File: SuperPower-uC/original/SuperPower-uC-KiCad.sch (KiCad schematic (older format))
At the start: 0 parts

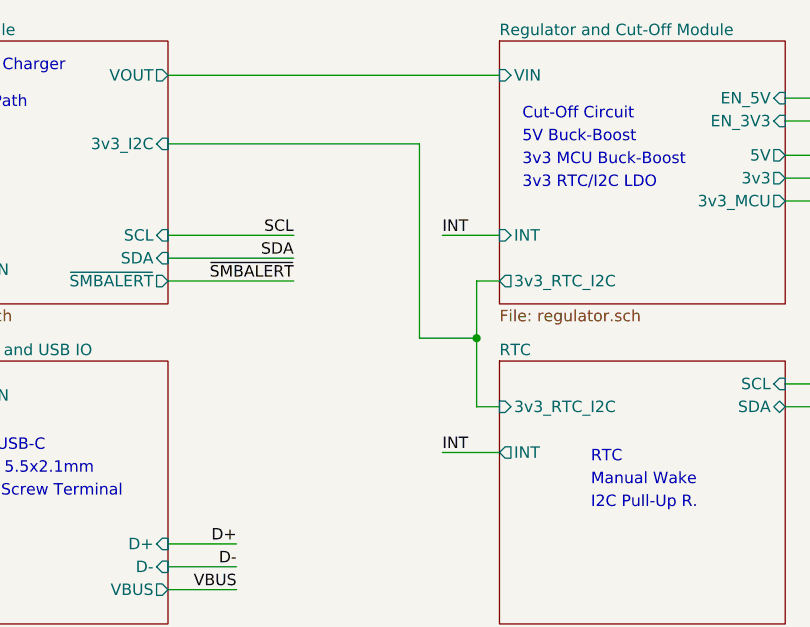
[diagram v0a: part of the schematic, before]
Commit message: Cleaned up the schematics and moved the I2C regulator to the RTC sheet
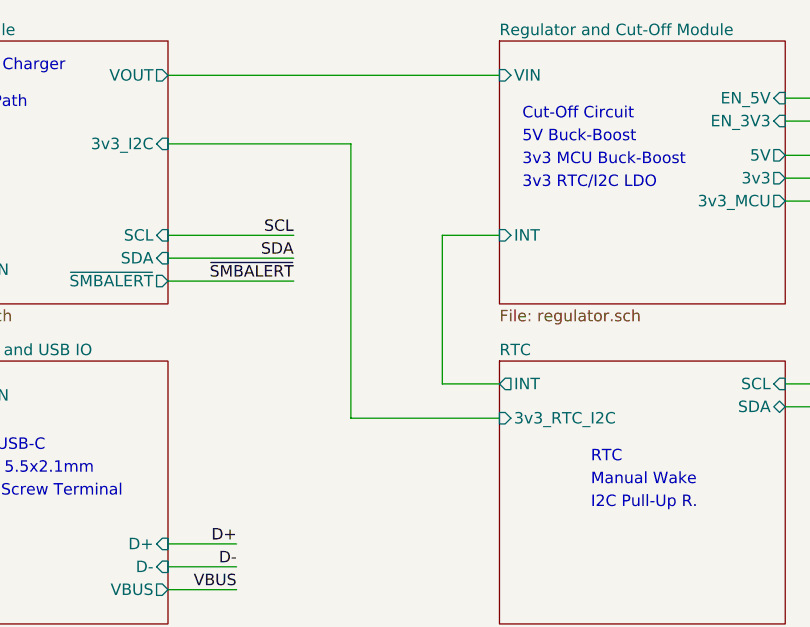
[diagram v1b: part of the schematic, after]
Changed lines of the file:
@@
 F2 "SCL" I R 7000 3600 50
 F3 "SDA" B R 7000 3700 50
-F4 "3v3_RTC_I2C" I L 5750 3700 50
-F5 "INT" O L 5750 3900 50
+F4 "3v3_RTC_I2C" I L 5750 3750 50
+F5 "INT" O L 5750 3600 50
 $EndSheet
 Wire Wire Line
@@
 Wire Wire Line
 	5750 2250 4300 2250
-Wire Wire Line
-	5400 2550 4300 2550
 Wire Wire Line
 	8600 2350 7000 2350
@@
 	10150 3150 9850 3150
 Wire Wire Line
-	5750 3700 5650 3700
-Wire Wire Line
-	5650 3700 5650 3400
-Wire Wire Line
-	5650 3150 5750 3150
-Wire Wire Line
-	5400 3400 5650 3400
-Wire Wire Line
-	5400 2550 5400 3400
-Connection ~ 5650 3400
-Wire Wire Line
-	5650 3400 5650 3150
-Text Label 5500 3900 0    50   ~ 0
-INT
-Wire Wire Line
-	5500 3900 5750 3900
-Text Label 5500 2950 0    50   ~ 0
-INT
+	5500 3600 5750 3600
 Wire Wire Line
 	5500 2950 5750 2950
@@
 F0 "Regulator and Cut-Off Module" 50
 F1 "regulator.sch" 50
-F2 "INT" I L 5750 2950 50
-F3 "3v3" O R 7000 2700 50
-F4 "5V" O R 7000 2600 50
-F5 "3v3_MCU" O R 7000 2800 50
-F6 "VIN" I L 5750 2250 50
-F7 "EN_3V3" I R 7000 2450 50
-F8 "EN_5V" I R 7000 2350 50
-F9 "3v3_RTC_I2C" O L 5750 3150 50
+F2 "3v3" O R 7000 2700 50
+F3 "5V" O R 7000 2600 50
+F4 "3v3_MCU" O R 7000 2800 50
+F5 "VIN" I L 5750 2250 50
+F6 "EN_3V3" I R 7000 2450 50
+F7 "EN_5V" I R 7000 2350 50
+F8 "INT" I L 5750 2950 50
 $EndSheet
 Text Notes 9100 2600 0    50   ~ 0
@@
 Text Notes 6150 4150 0    50   ~ 0
 I2C Pull-Up R.
+Wire Wire Line
+	5100 2550 4300 2550
+Wire Wire Line
+	5750 3750 5100 3750
+Wire Wire Line
+	5100 2550 5100 3750
+Wire Wire Line
+	5500 3600 5500 2950
 $EndSCHEMATC

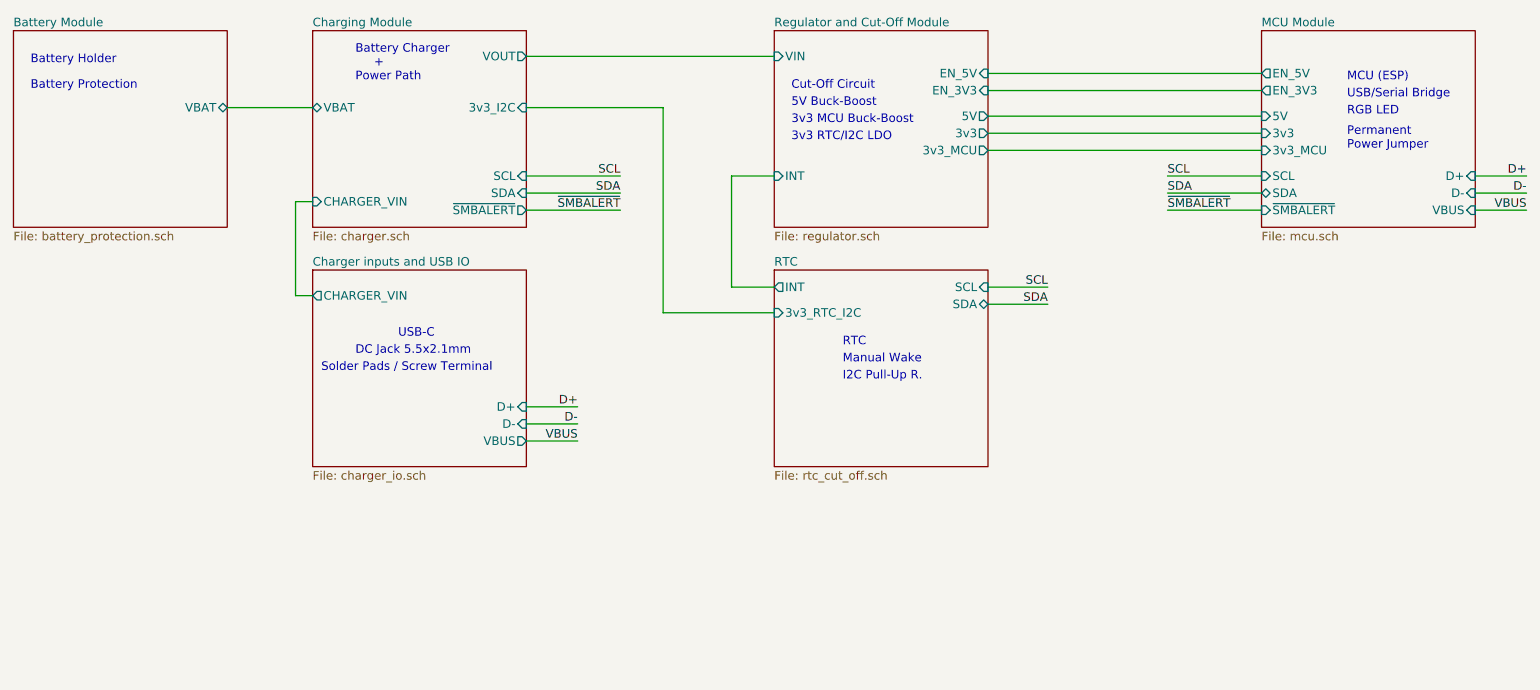
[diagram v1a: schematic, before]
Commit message: Layed out IO sheet parts
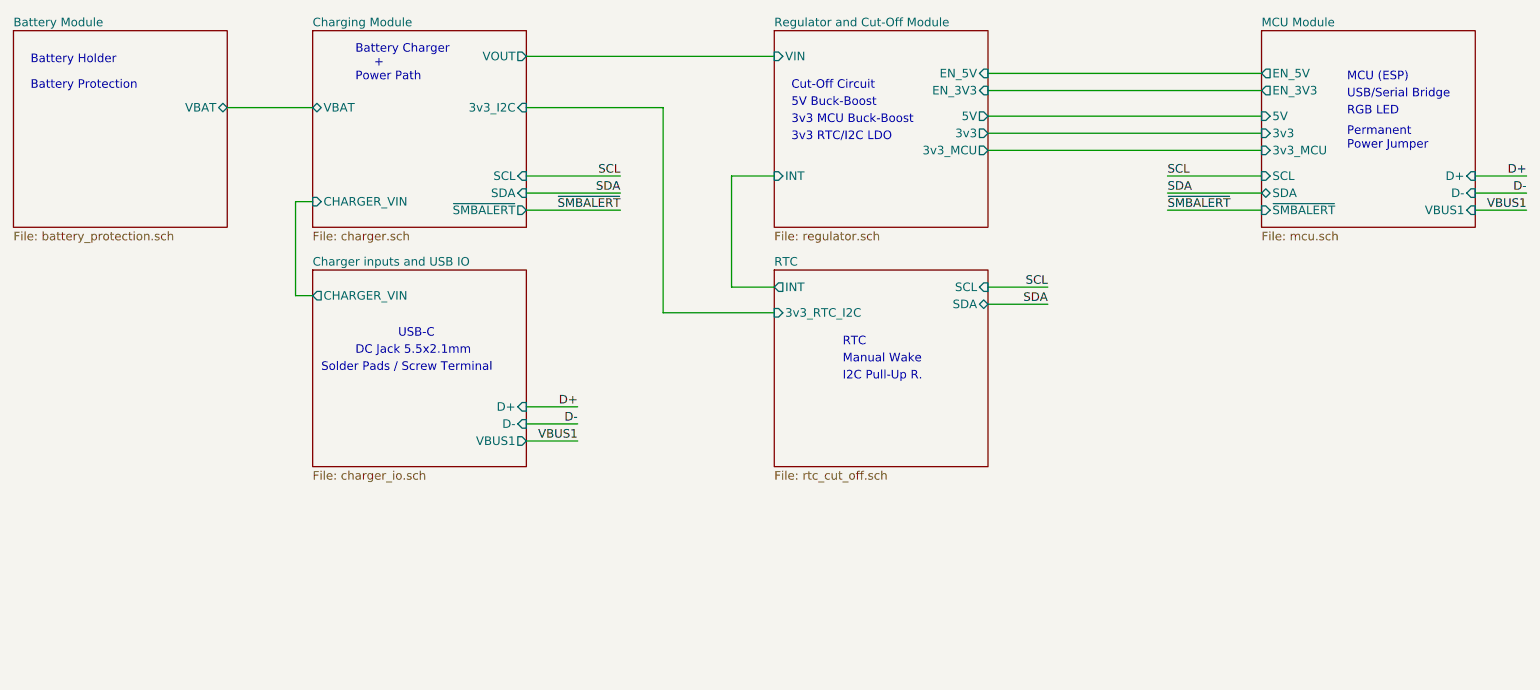
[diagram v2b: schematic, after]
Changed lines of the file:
@@
 F0 "Charger inputs and USB IO" 50
 F1 "charger_io.sch" 50
-F2 "VBUS" O R 4300 4500 50
-F3 "D+" I R 4300 4300 50
-F4 "D-" I R 4300 4400 50
-F5 "CHARGER_VIN" O L 3050 3650 50
+F2 "D+" I R 4300 4300 50
+F3 "D-" I R 4300 4400 50
+F4 "CHARGER_VIN" O L 3050 3650 50
+F5 "VBUS1" O R 4300 4500 50
 $EndSheet
 Wire Wire Line
@@
 	4850 3150 4300 3150
 Text Label 4600 4500 2    50   ~ 0
-VBUS
+VBUS1
 Text Label 4600 4400 2    50   ~ 0
 D-
@@
 	4600 4500 4300 4500
 Text Label 10150 3150 2    50   ~ 0
-VBUS
+VBUS1
 Text Label 10150 3050 2    50   ~ 0
 D-
@@
 F5 "D+" I R 9850 2950 50
 F6 "D-" I R 9850 3050 50
-F7 "VBUS" I R 9850 3150 50
-F8 "5V" I L 8600 2600 50
-F9 "3v3" I L 8600 2700 50
-F10 "EN_3V3" O L 8600 2450 50
-F11 "EN_5V" O L 8600 2350 50
-F12 "~SMBALERT" I L 8600 3150 50
+F7 "5V" I L 8600 2600 50
+F8 "3v3" I L 8600 2700 50
+F9 "EN_3V3" O L 8600 2450 50
+F10 "EN_5V" O L 8600 2350 50
+F11 "~SMBALERT" I L 8600 3150 50
+F12 "VBUS1" I R 9850 3150 50
 $EndSheet
 $Sheet

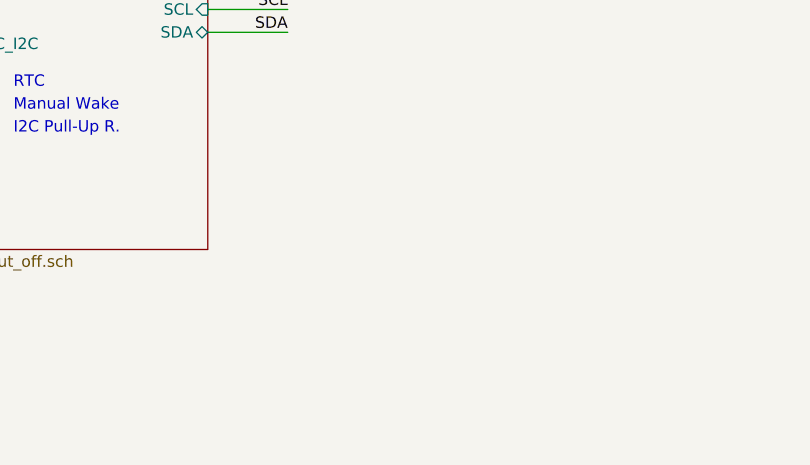
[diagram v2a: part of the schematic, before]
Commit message: draft of the squared stackable version
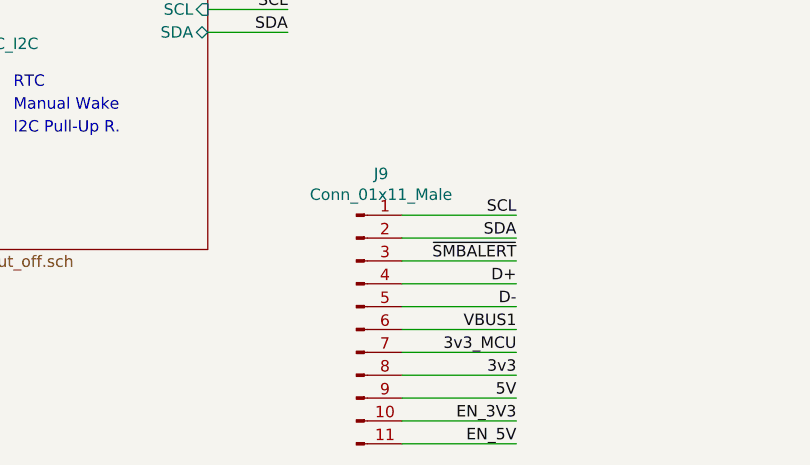
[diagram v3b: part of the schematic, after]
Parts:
- added J9: Conn_01x11_Male, Connector_PinSocket_2.54mm:PinSocket_1x11_P2.54mm_Vertical, symbol Connector:Conn_01x11_Male
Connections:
- net D+: now also J9.4 (Pin_4)
- net D-: now also J9.5 (Pin_5)
- net SCL: now also J9.1 (Pin_1)
- net SDA: now also J9.2 (Pin_2)
- net VBUS1: now also J9.6 (Pin_6)
- net ~SMBALERT: now also J9.3 (Pin_3)
- new net 3v3: J9.8 (Pin_8)
- new net 3v3_MCU: J9.7 (Pin_7)
- new net 5V: J9.9 (Pin_9)
- new net EN_3V3: J9.10 (Pin_10)
- new net EN_5V: J9.11 (Pin_11)
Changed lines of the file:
@@
 Wire Wire Line
 	5500 3600 5500 2950
+$Comp
+L Connector:Conn_01x11_Male J9
+U 1 1 60000B18
+P 7650 5000
+F 0 "J9" H 7758 5681 50  0000 C CNN
+F 1 "Conn_01x11_Male" H 7758 5590 50  0000 C CNN
+F 2 "Connector_PinSocket_2.54mm:PinSocket_1x11_P2.54mm_Vertical" H 7650 5000 50  0001 C CNN
+F 3 "~" H 7650 5000 50  0001 C CNN
+	1    7650 5000
+	1    0    0    -1
+$EndComp
+Text Label 8350 4500 2    50   ~ 0
+SCL
+Text Label 8350 4600 2    50   ~ 0
+SDA
+Text Label 8350 4700 2    50   ~ 0
+~SMBALERT
+Text Label 8350 4800 2    50   ~ 0
+D+
+Text Label 8350 4900 2    50   ~ 0
+D-
+Text Label 8350 5000 2    50   ~ 0
+VBUS1
+Text Label 8350 5200 2    50   ~ 0
+3v3
+Text Label 8350 5500 2    50   ~ 0
+EN_5V
+Text Label 8350 5400 2    50   ~ 0
+EN_3V3
+Text Label 8350 5300 2    50   ~ 0
+5V
+Text Label 8350 5100 2    50   ~ 0
+3v3_MCU
+Wire Wire Line
+	7850 4500 8350 4500
+Wire Wire Line
+	8350 4600 7850 4600
+Wire Wire Line
+	7850 4700 8350 4700
+Wire Wire Line
+	8350 4800 7850 4800
+Wire Wire Line
+	7850 4900 8350 4900
+Wire Wire Line
+	8350 5000 7850 5000
+Wire Wire Line
+	7850 5100 8350 5100
+Wire Wire Line
+	8350 5200 7850 5200
+Wire Wire Line
+	7850 5300 8350 5300
+Wire Wire Line
+	8350 5400 7850 5400
+Wire Wire Line
+	7850 5500 8350 5500
 $EndSCHEMATC

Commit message: Layed out the whole charger board
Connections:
- net 3v3: now also J9.10 (Pin_10); no longer J9.8 (Pin_8)
- net 3v3_MCU: now also J9.9 (Pin_9); no longer J9.7 (Pin_7)
- net 5V: now also J9.7 (Pin_7); no longer J9.9 (Pin_9)
- net EN_3V3: now also J9.8 (Pin_8); no longer J9.10 (Pin_10)
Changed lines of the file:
@@
 Text Label 8350 5000 2    50   ~ 0
 VBUS1
-Text Label 8350 5200 2    50   ~ 0
+Text Label 8350 5400 2    50   ~ 0
 3v3
 Text Label 8350 5500 2    50   ~ 0
 EN_5V
-Text Label 8350 5400 2    50   ~ 0
+Text Label 8350 5200 2    50   ~ 0
 EN_3V3
+Text Label 8350 5100 2    50   ~ 0
+5V
 Text Label 8350 5300 2    50   ~ 0
-5V
-Text Label 8350 5100 2    50   ~ 0
 3v3_MCU
 Wire Wire Line
@@
 Wire Wire Line
 	7850 5500 8350 5500
+Text Label 8300 2350 2    50   ~ 0
+EN_5V
+Text Label 8300 2450 2    50   ~ 0
+EN_3V3
+Text Label 8300 2600 2    50   ~ 0
+5V
+Text Label 8300 2700 2    50   ~ 0
+3v3
+Text Label 8300 2800 2    50   ~ 0
+3v3_MCU
 $EndSCHEMATC

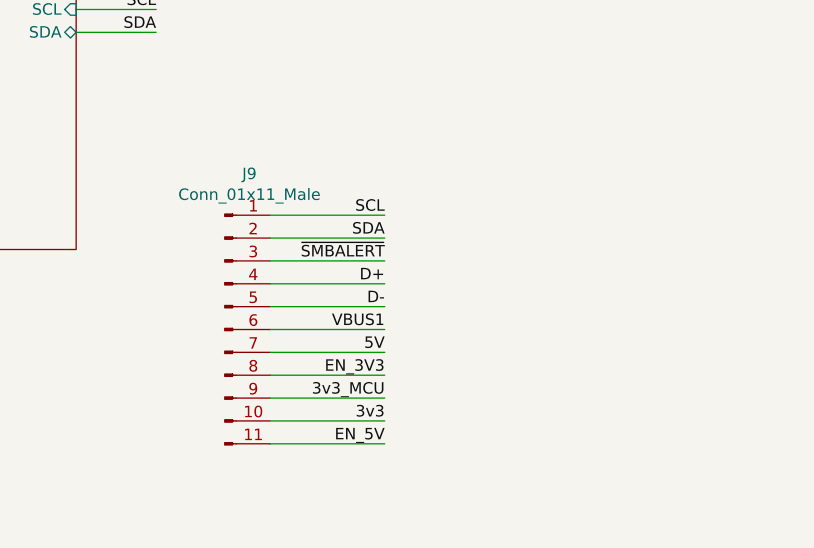
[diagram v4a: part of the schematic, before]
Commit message: Layed out mcu board
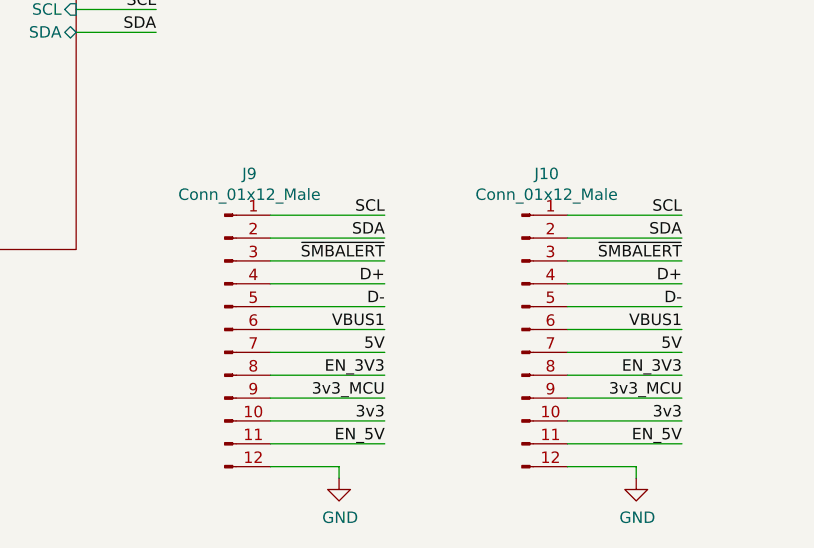
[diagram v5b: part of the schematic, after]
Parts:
- removed J9: Conn_01x11_Male, Connector_PinSocket_2.54mm:PinSocket_1x11_P2.54mm_Vertical, symbol Connector:Conn_01x11_Male
- added J10, J9: Conn_01x12_Male, Connector_PinSocket_2.54mm:PinSocket_1x12_P2.54mm_Vertical, symbol Connector:Conn_01x12_Male
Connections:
- net 3v3: now also J10.10 (Pin_10), J9.10 (Pin_10)
- net 3v3_MCU: now also J10.9 (Pin_9), J9.9 (Pin_9)
- net 5V: now also J10.7 (Pin_7), J9.7 (Pin_7)
- net D+: now also J10.4 (Pin_4), J9.4 (Pin_4)
- net D-: now also J10.5 (Pin_5), J9.5 (Pin_5)
- net EN_3V3: now also J10.8 (Pin_8), J9.8 (Pin_8)
- net EN_5V: now also J10.11 (Pin_11), J9.11 (Pin_11)
- net SCL: now also J10.1 (Pin_1), J9.1 (Pin_1)
- net SDA: now also J10.2 (Pin_2), J9.2 (Pin_2)
- net VBUS1: now also J10.6 (Pin_6), J9.6 (Pin_6)
- net ~SMBALERT: now also J10.3 (Pin_3), J9.3 (Pin_3)
- new net GND: J10.12 (Pin_12), J9.12 (Pin_12)
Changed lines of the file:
@@
 Wire Wire Line
 	5500 3600 5500 2950
-$Comp
-L Connector:Conn_01x11_Male J9
-U 1 1 60000B18
-P 7650 5000
-F 0 "J9" H 7758 5681 50  0000 C CNN
-F 1 "Conn_01x11_Male" H 7758 5590 50  0000 C CNN
-F 2 "Connector_PinSocket_2.54mm:PinSocket_1x11_P2.54mm_Vertical" H 7650 5000 50  0001 C CNN
-F 3 "~" H 7650 5000 50  0001 C CNN
-	1    7650 5000
-	1    0    0    -1
-$EndComp
 Text Label 8350 4500 2    50   ~ 0
 SCL
@@
 Text Label 8300 2800 2    50   ~ 0
 3v3_MCU
+$Comp
+L Connector:Conn_01x12_Male J9
+U 1 1 5FE4755E
+P 7650 5000
+F 0 "J9" H 7758 5681 50  0000 C CNN
+F 1 "Conn_01x12_Male" H 7758 5590 50  0000 C CNN
+F 2 "Connector_PinSocket_2.54mm:PinSocket_1x12_P2.54mm_Vertical" H 7650 5000 50  0001 C CNN
+F 3 "~" H 7650 5000 50  0001 C CNN
+	1    7650 5000
+	1    0    0    -1
+$EndComp
+$Comp
+L power:GND #PWR0112
+U 1 1 5FE48E31
+P 8150 5650
+F 0 "#PWR0112" H 8150 5400 50  0001 C CNN
+F 1 "GND" H 8155 5477 50  0000 C CNN
+F 2 "" H 8150 5650 50  0001 C CNN
+F 3 "" H 8150 5650 50  0001 C CNN
+	1    8150 5650
+	1    0    0    -1
+$EndComp
+Wire Wire Line
+	8150 5650 8150 5600
+Wire Wire Line
+	8150 5600 7850 5600
+$Comp
+L Connector:Conn_01x12_Male J10
+U 1 1 5FE627D1
+P 8950 5000
+F 0 "J10" H 9058 5681 50  0000 C CNN
+F 1 "Conn_01x12_Male" H 9058 5590 50  0000 C CNN
+F 2 "Connector_PinSocket_2.54mm:PinSocket_1x12_P2.54mm_Vertical" H 8950 5000 50  0001 C CNN
+F 3 "~" H 8950 5000 50  0001 C CNN
+	1    8950 5000
+	1    0    0    -1
+$EndComp
+Text Label 9650 4500 2    50   ~ 0
+SCL
+Text Label 9650 4600 2    50   ~ 0
+SDA
+Text Label 9650 4700 2    50   ~ 0
+~SMBALERT
+Text Label 9650 4800 2    50   ~ 0
+D+
+Text Label 9650 4900 2    50   ~ 0
+D-
+Text Label 9650 5000 2    50   ~ 0
+VBUS1
+Text Label 9650 5400 2    50   ~ 0
+3v3
+Text Label 9650 5500 2    50   ~ 0
+EN_5V
+Text Label 9650 5200 2    50   ~ 0
+EN_3V3
+Text Label 9650 5100 2    50   ~ 0
+5V
+Text Label 9650 5300 2    50   ~ 0
+3v3_MCU
+Wire Wire Line
+	9150 4500 9650 4500
+Wire Wire Line
+	9650 4600 9150 4600
+Wire Wire Line
+	9150 4700 9650 4700
+Wire Wire Line
+	9650 4800 9150 4800
+Wire Wire Line
+	9150 4900 9650 4900
+Wire Wire Line
+	9650 5000 9150 5000
+Wire Wire Line
+	9150 5100 9650 5100
+Wire Wire Line
+	9650 5200 9150 5200
+Wire Wire Line
+	9150 5300 9650 5300
+Wire Wire Line
+	9650 5400 9150 5400
+Wire Wire Line
+	9150 5500 9650 5500
+$Comp
+L power:GND #PWR0113
+U 1 1 5FE66948
+P 9450 5650
+F 0 "#PWR0113" H 9450 5400 50  0001 C CNN
+F 1 "GND" H 9455 5477 50  0000 C CNN
+F 2 "" H 9450 5650 50  0001 C CNN
+F 3 "" H 9450 5650 50  0001 C CNN
+	1    9450 5650
+	1    0    0    -1
+$EndComp
+Wire Wire Line
+	9450 5650 9450 5600
+Wire Wire Line
+	9450 5600 9150 5600
 $EndSCHEMATC
